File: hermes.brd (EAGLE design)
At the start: 22.9 x 35.1 mm, 36 parts

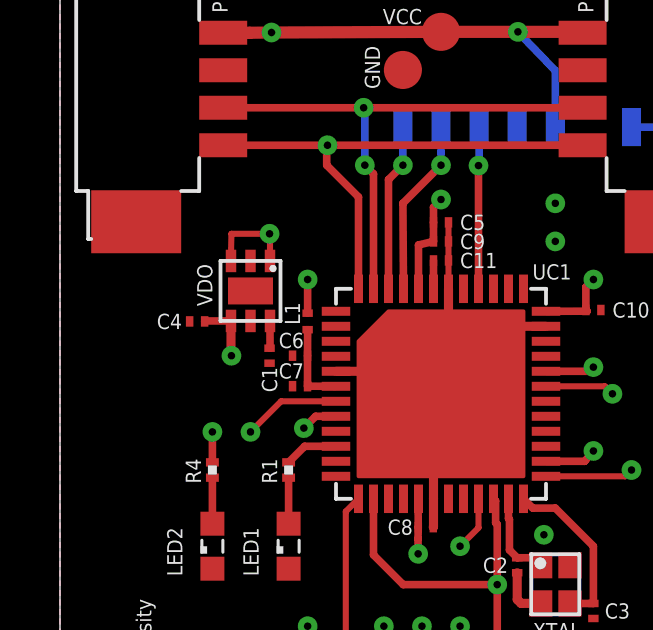
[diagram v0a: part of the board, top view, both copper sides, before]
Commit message: Alternative version with LDO TS9013
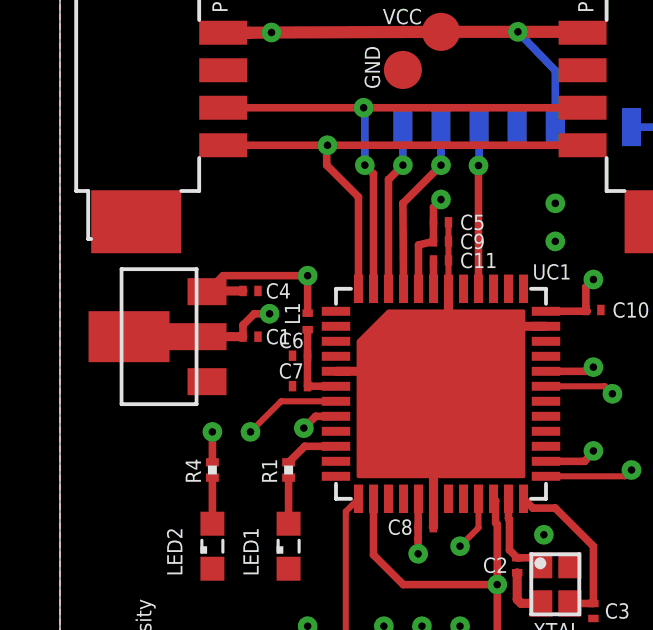
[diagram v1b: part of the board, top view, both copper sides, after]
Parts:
- removed VDO: MIC5219-3.3BML, Hermes_lib:MLF-6
- added U$1: TS9013SCY RMG, Hermes_lib:SOT-89
- C1: value 470pF -> 1uF
- moved C4 2.05 mm to (43.2, 32.6), turned to 0 degrees
- moved C1 0.90 mm to (43.2, 31.1), turned to 0 degrees
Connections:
- removed net N$2: C1.1, VDO.P$6
- net +3V3: now also U$1.OUT; no longer VDO.P$4
- net GND: now also U$1.GND; no longer VDO.P$2, VDO.P$7
- net VCC: now also C1.1, U$1.IN, U$1.IN_DRAIN; no longer VDO.P$1, VDO.P$3
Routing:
- net VCC: track 25.5 -> 30.3 mm
- net +3V3: track 23.4 -> 26.3 mm, vias 14 -> 13
- net N$2: track 0.92 -> 0.00 mm
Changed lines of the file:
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@@
 <layer number="17" name="Pads" color="2" fill="1" visible="no" active="yes"/>
 <layer number="18" name="Vias" color="2" fill="1" visible="yes" active="yes"/>
-<layer number="19" name="Unrouted" color="6" fill="1" visible="no" active="yes"/>
+<layer number="19" name="Unrouted" color="6" fill="1" visible="yes" active="yes"/>
 <layer number="20" name="Dimension" color="24" fill="1" visible="yes" active="yes"/>
 <layer number="21" name="tPlace" color="7" fill="1" visible="yes" active="yes"/>
@@
 </autorouter>
 <elements>
-<element name="C1" library="rcl" library_urn="urn:adsk.eagle:library:334" package="C0201" package3d_urn="urn:adsk.eagle:package:23690/1" value="470pF" x="43.815" y="30.48" smashed="yes" rot="R270">
-<attribute name="NAME" x="43.561" y="30.099" size="0.508" layer="25" rot="R270"/>
-<attribute name="VALUE" x="41.91" y="31.115" size="0.508" layer="27" rot="R270"/>
+<element name="C1" library="rcl" library_urn="urn:adsk.eagle:library:334" package="C0201" package3d_urn="urn:adsk.eagle:package:23690/1" value="1uF" x="43.18" y="31.115" smashed="yes">
+<attribute name="NAME" x="43.688" y="30.861" size="0.508" layer="25"/>
+<attribute name="VALUE" x="42.545" y="29.21" size="0.508" layer="27"/>
 </element>
 <element name="C10" library="rcl" library_urn="urn:adsk.eagle:library:334" package="C0201" package3d_urn="urn:adsk.eagle:package:23690/1" value="100nF" x="54.61" y="32.004" smashed="yes">
@@
 <attribute name="VALUE" x="52.705" y="22.606" size="0.508" layer="27" rot="R270"/>
 </element>
-<element name="C4" library="rcl" library_urn="urn:adsk.eagle:library:334" package="C0201" package3d_urn="urn:adsk.eagle:package:23690/1" value="2.2uF" x="41.402" y="31.623" smashed="yes" rot="R180">
-<attribute name="NAME" x="40.894" y="31.877" size="0.508" layer="25" rot="R180"/>
-<attribute name="VALUE" x="42.037" y="33.528" size="0.508" layer="27" rot="R180"/>
+<element name="C4" library="rcl" library_urn="urn:adsk.eagle:library:334" package="C0201" package3d_urn="urn:adsk.eagle:package:23690/1" value="2.2uF" x="43.18" y="32.639" smashed="yes">
+<attribute name="NAME" x="43.688" y="32.385" size="0.508" layer="25"/>
+<attribute name="VALUE" x="42.545" y="30.734" size="0.508" layer="27"/>
 </element>
 <element name="C5" library="rcl" library_urn="urn:adsk.eagle:library:334" package="C0201" package3d_urn="urn:adsk.eagle:package:23690/1" value="10uF" x="49.53" y="34.925" smashed="yes">
@@
 <element name="PEER2" library="Hermes_lib" package="PICO-BLADE4" value="PICO-BLADE4" x="57.15" y="39.37" smashed="yes" rot="R90">
 <attribute name="NAME" x="54.61" y="41.91" size="0.508" layer="25" rot="R90"/>
-</element>
-<element name="VDO" library="Hermes_lib" package="MLF-6" value="MIC5219-3.3BML" x="43.18" y="32.639" smashed="yes" rot="R270">
-<attribute name="NAME" x="41.91" y="32.131" size="0.508" layer="25" rot="R90"/>
-<attribute name="VALUE" x="41.68" y="33.639" size="0.508" layer="27" rot="R270"/>
 </element>
 <element name="L1" library="rcl" library_urn="urn:adsk.eagle:library:334" package="L0201" package3d_urn="urn:adsk.eagle:package:23513/1" value="10uH" x="45.085" y="31.623" smashed="yes" rot="R270">
@@
 <attribute name="NAME" x="52.594" y="21.062" size="0.508" layer="25"/>
 <attribute name="VALUE" x="51.59" y="23.86" size="0.4064" layer="27" rot="R270"/>
+</element>
+<element name="U$1" library="Hermes_lib" package="SOT-89" value="TS9013SCY RMG " x="40.132" y="31.115" smashed="yes" rot="R90">
+<attribute name="NAME" x="31.432" y="30.655" size="1.27" layer="25" rot="R90"/>
+<attribute name="NAME" x="46.132" y="28.115" size="1.27" layer="27" rot="R90"/>
 </element>
 </elements>
@@
 <contactref element="C8" pad="1"/>
 <contactref element="L1" pad="1"/>
-<contactref element="VDO" pad="P$4"/>
 <contactref element="C4" pad="1"/>
 <contactref element="R4" pad="1"/>
@@
 <contactref element="R5" pad="2"/>
 <contactref element="SLAVE" pad="P$9"/>
-<wire x1="41.668" y1="31.639" x2="42.53" y2="31.639" width="0.254" layer="1"/>
-<wire x1="41.668" y1="31.639" x2="41.652" y2="31.623" width="0.254" layer="1"/>
 <polygon width="0.3048" layer="2">
 <vertex x="36.83" y="46.355"/>
@@
 <vertex x="59.69" y="46.355"/>
 </polygon>
-<wire x1="42.53" y1="31.639" x2="42.53" y2="30.495" width="0.3048" layer="1"/>
-<wire x1="42.53" y1="30.495" x2="42.545" y2="30.48" width="0.3048" layer="1"/>
-<via x="42.545" y="30.48" extent="1-16" drill="0.25"/>
 <wire x1="52.655" y1="16.743" x2="52.655" y2="18.873" width="0.3048" layer="1"/>
 <wire x1="52.655" y1="18.873" x2="52.705" y2="18.923" width="0.3048" layer="1"/>
@@
 <wire x1="49.28" y1="34.29" x2="49.28" y2="34.925" width="0.254" layer="1"/>
 <via x="49.53" y="35.687" extent="1-16" drill="0.25"/>
-<wire x1="45.085" y1="31.898" x2="45.085" y2="33.02" width="0.254" layer="1"/>
-<via x="45.085" y="33.02" extent="1-16" drill="0.25"/>
+<wire x1="45.085" y1="31.898" x2="45.085" y2="33.147" width="0.254" layer="1"/>
+<via x="45.085" y="33.147" extent="1-16" drill="0.25"/>
 <wire x1="53.03" y1="31.96" x2="54.4" y2="31.964" width="0.254" layer="1"/>
 <wire x1="54.4" y1="31.964" x2="54.36" y2="32.004" width="0.254" layer="1"/>
@@
 <wire x1="49.656" y1="20.067" x2="49.53" y2="20.193" width="0.254" layer="1"/>
 <via x="49.53" y="20.193" extent="1-16" drill="0.25"/>
+<contactref element="U$1" pad="OUT"/>
+<wire x1="42.93" y1="32.639" x2="41.756" y2="32.639" width="0.3048" layer="1"/>
+<wire x1="41.732" y1="32.615" x2="41.756" y2="32.639" width="0.3048" layer="1"/>
+<wire x1="45.085" y1="33.147" x2="42.264" y2="33.147" width="0.254" layer="1"/>
+<wire x1="42.264" y1="33.147" x2="41.732" y2="32.615" width="0.254" layer="1"/>
 </signal>
 <signal name="GND">
@@
 <contactref element="C8" pad="2"/>
 <contactref element="C4" pad="2"/>
-<contactref element="VDO" pad="P$2"/>
 <contactref element="LED1" pad="C"/>
 <contactref element="LED2" pad="C"/>
 <contactref element="C2" pad="2"/>
 <contactref element="C3" pad="2"/>
-<contactref element="C1" pad="2"/>
 <contactref element="XTAL" pad="GND@2"/>
 <contactref element="XTAL" pad="GND@1"/>
@@
 <vertex x="59.69" y="46.355"/>
 </polygon>
-<contactref element="VDO" pad="P$7"/>
 <wire x1="49.28" y1="28.96" x2="49.28" y2="25.71" width="0.3048" layer="1"/>
 <wire x1="49.53" y1="29.21" x2="49.28" y2="28.96" width="0.3048" layer="1"/>
@@
 <vertex x="59.69" y="11.303"/>
 </polygon>
+<contactref element="C1" pad="2"/>
+<contactref element="U$1" pad="GND"/>
 </signal>
 <signal name="VCC">
-<contactref element="VDO" pad="P$3"/>
-<contactref element="VDO" pad="P$1"/>
 <contactref element="PIN1" pad="P$1"/>
 <contactref element="VCC" pad="TP"/>
@@
 <wire x1="53.34" y1="39.982140625" x2="52.092859375" y2="41.275" width="0.254" layer="16"/>
 <via x="52.092859375" y="41.275" extent="1-16" drill="0.25"/>
-<via x="43.815" y="34.544" extent="1-16" drill="0.25"/>
+<via x="43.815" y="31.877" extent="1-16" drill="0.25"/>
 <via x="43.880634375" y="41.25324375" extent="1-16" drill="0.25"/>
-<wire x1="42.53" y1="33.639" x2="42.53" y2="33.894" width="0.2032" layer="1"/>
-<wire x1="42.53" y1="33.894" x2="42.545" y2="34.544" width="0.2032" layer="1"/>
-<wire x1="43.815" y1="34.544" x2="42.545" y2="34.544" width="0.2032" layer="1"/>
-<wire x1="43.83" y1="33.639" x2="43.83" y2="34.529" width="0.2032" layer="1"/>
-<wire x1="43.83" y1="34.529" x2="43.815" y2="34.544" width="0.2032" layer="1"/>
 <wire x1="43.815" y1="41.187609375" x2="43.880634375" y2="41.25324375" width="0.254" layer="2"/>
-<wire x1="43.815" y1="34.544" x2="43.815" y2="41.187609375" width="0.254" layer="2"/>
+<wire x1="43.815" y1="31.877" x2="43.815" y2="41.187609375" width="0.254" layer="2"/>
+<contactref element="U$1" pad="IN"/>
+<contactref element="U$1" pad="IN_DRAIN"/>
+<contactref element="C1" pad="1"/>
+<wire x1="41.432" y1="31.115" x2="42.93" y2="31.115" width="0.3048" layer="1"/>
+<wire x1="42.93" y1="31.115" x2="42.93" y2="31.5" width="0.254" layer="1"/>
+<wire x1="42.93" y1="31.5" x2="43.307" y2="31.877" width="0.254" layer="1"/>
+<wire x1="43.307" y1="31.877" x2="43.815" y2="31.877" width="0.254" layer="1"/>
+<wire x1="39.132" y1="31.115" x2="41.432" y2="31.115" width="0.254" layer="1"/>
 </signal>
 <signal name="LED">
@@
 <via x="46.95126875" y="38.745" extent="1-16" drill="0.25"/>
 </signal>
-<signal name="N$2">
-<contactref element="VDO" pad="P$6"/>
-<contactref element="C1" pad="1"/>
-<wire x1="43.83" y1="31.639" x2="43.831" y2="30.746" width="0.254" layer="1"/>
-<wire x1="43.831" y1="30.746" x2="43.815" y2="30.73" width="0.254" layer="1"/>
-</signal>
 <signal name="N$3">
